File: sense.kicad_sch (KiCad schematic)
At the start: 36 parts, among them J6 Rudder, J7 End Stops, J8 Conn_01x02, J9 ISP, U4 XC6202P502FR-G, U6 LM317, U7 ATmega328P-AU, Y1 8mhz

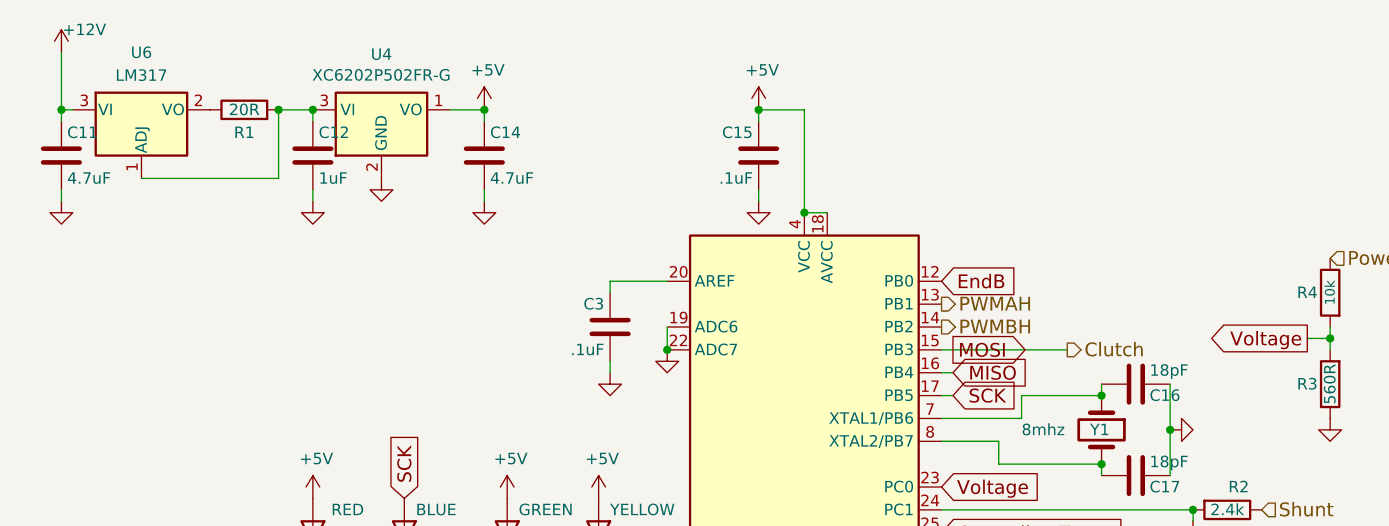
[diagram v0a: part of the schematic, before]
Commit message: Fixed almost all ERC errors and warnings (now 0 errors, 3 warnings)
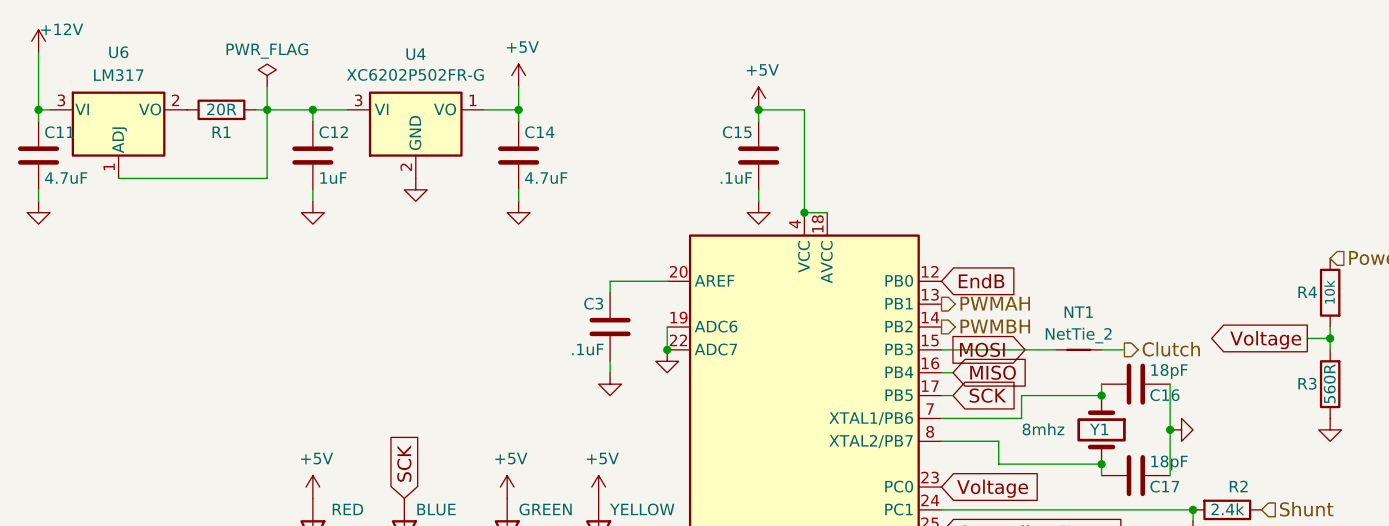
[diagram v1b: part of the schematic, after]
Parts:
- added NT1: NetTie_2, NetTie:NetTie-2_SMD_Pad0.5mm, symbol Device:NetTie_2
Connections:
- net MOSI: now also NT1.1
- new net Clutch: NT1.2
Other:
- moved on the sheet: C11, C14, R1, U4, U6

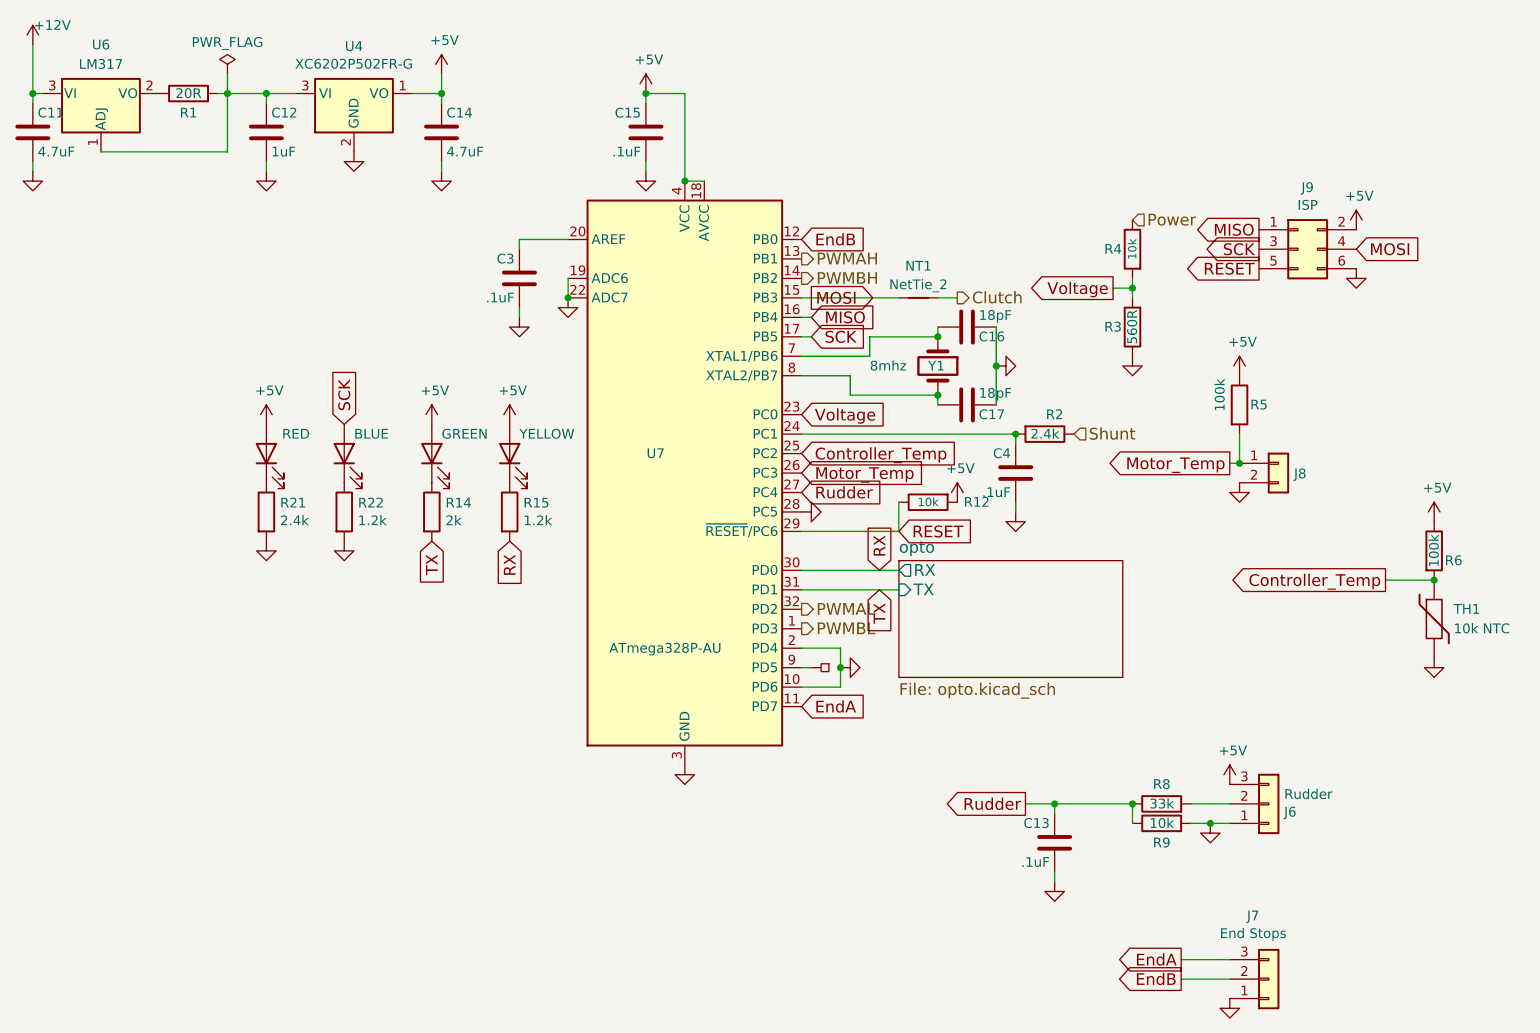
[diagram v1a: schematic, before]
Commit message: Cleaned LCSC part numbers out of datasheet field (and renamed 0.1u to 100n)
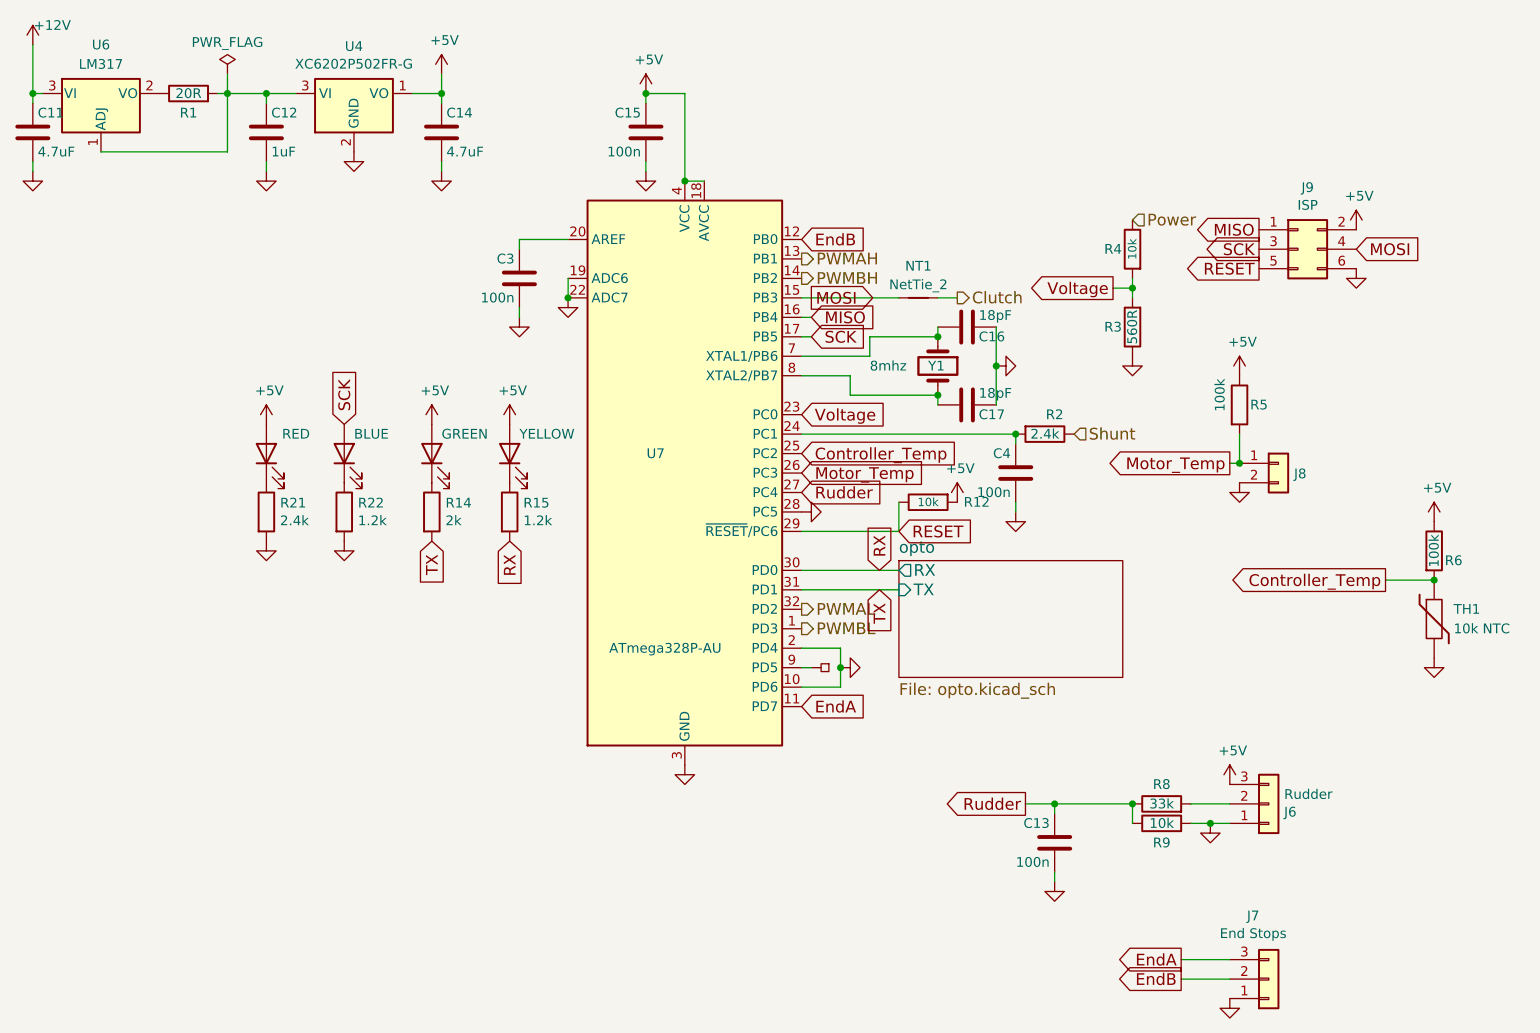
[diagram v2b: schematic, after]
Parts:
- C13, C15, C3, C4: value .1uF -> 100n
- TH1: LCSC C72672 -> *C72672, C51597
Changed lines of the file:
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@@
 			)
 		)
-		(property "Datasheet" "C51597, C72672"
+		(property "Datasheet" "~"
 			(at 218.44 100.33 0)
 			(effects
@@
 			)
 		)
-		(property "LCSC" "C72672"
+		(property "LCSC" "*C72672, C51597"
 			(at 218.44 100.33 0)
 			(effects
@@
 			)
 		)
-		(property "Value" ".1uF"
+		(property "Value" "100n"
 			(at 98.425 58.42 0)
 			(effects
@@
 			)
 		)
-		(property "Value" ".1uF"
+		(property "Value" "100n"
 			(at 114.935 39.37 0)
 			(effects
@@
 			)
 		)
-		(property "Value" ".1uF"
+		(property "Value" "100n"
 			(at 163.195 83.82 0)
 			(effects
@@
 			)
 		)
-		(property "Value" ".1uF"
+		(property "Value" "100n"
 			(at 168.275 132.08 0)
 			(effects

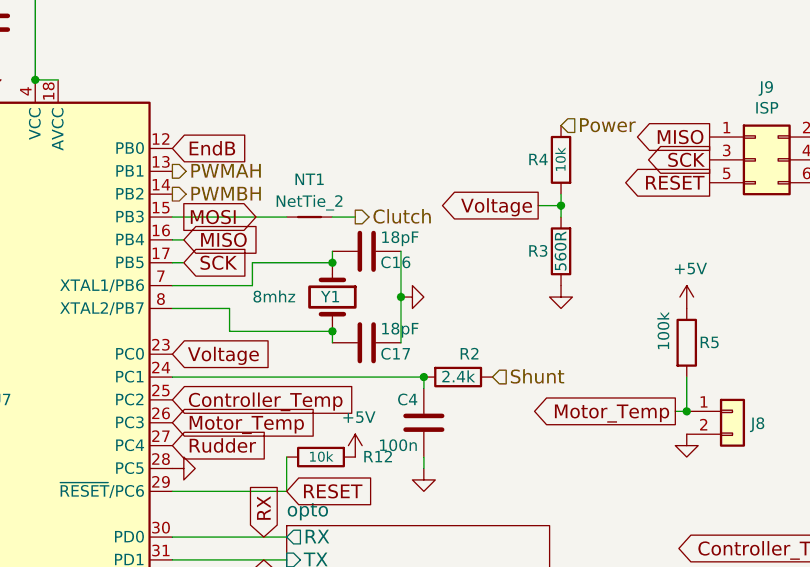
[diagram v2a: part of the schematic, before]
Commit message: Replace crystal caps with a JLC PCBA basic part (20pF instead of 18pF)
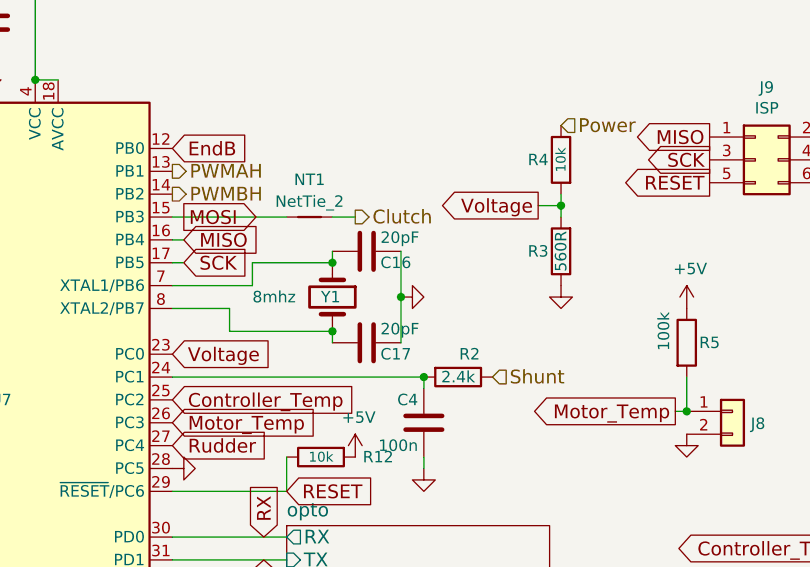
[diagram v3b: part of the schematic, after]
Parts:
- C16, C17: value 18pF -> 20pF; LCSC C1797 -> C1798
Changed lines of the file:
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@@
 			)
 		)
-		(property "Value" "18pF"
+		(property "Value" "20pF"
 			(at 159.004 70.866 90)
 			(effects
@@
 			)
 		)
-		(property "LCSC" "C1797"
+		(property "LCSC" "C1798"
 			(at 157.48 72.39 90)
 			(effects
@@
 			)
 		)
-		(property "Value" "18pF"
+		(property "Value" "20pF"
 			(at 159.004 60.706 90)
 			(effects
@@
 			)
 		)
-		(property "LCSC" "C1797"
+		(property "LCSC" "C1798"
 			(at 157.48 62.23 90)
 			(effects

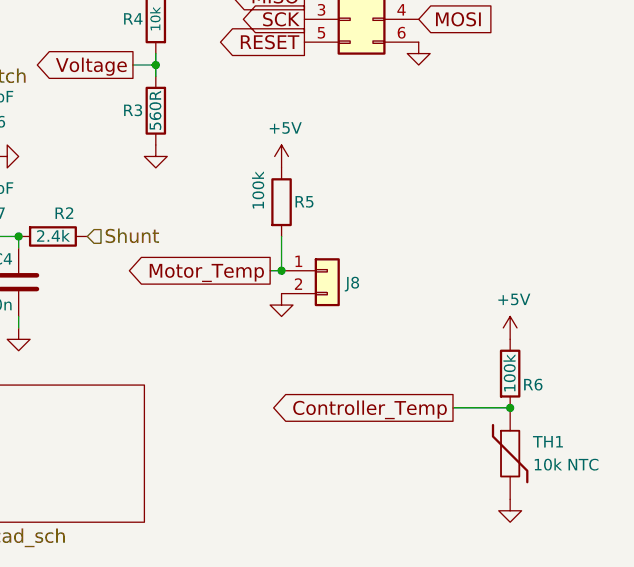
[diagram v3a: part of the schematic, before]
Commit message: Show motor temp on J8, the motor temp connector
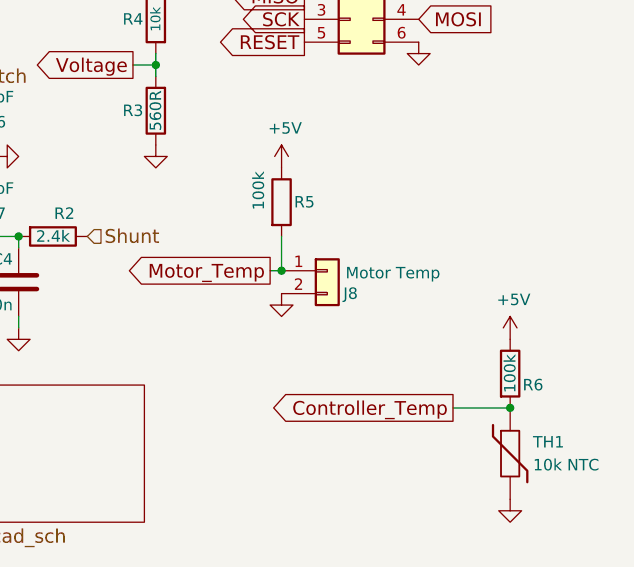
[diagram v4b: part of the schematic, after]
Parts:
- J8: value Conn_01x02 -> Motor Temp
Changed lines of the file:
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@@
 		(dnp no)
 		(property "Reference" "J8"
-			(at 200.152 81.3816 0)
+			(at 199.898 82.55 0)
 			(effects
 				(font
@@
 			)
 		)
-		(property "Value" "Conn_01x02"
-			(at 200.152 82.5246 0)
+		(property "Value" "Motor Temp"
+			(at 200.152 80.264 0)
 			(effects
 				(font
@@
 				)
 				(justify left)
-				(hide yes)
 			)
 		)

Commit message: Add MOSFET to switch a relay on the clutch output
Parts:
- J6, J7: LCSC (none) -> C19190477
- J8: LCSC (none) -> C7434479
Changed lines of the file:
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@@
+			)
+		)
+		(property "LCSC" "C7434479"
+			(at 198.12 80.01 0)
+			(effects
+				(font
+					(size 1.27 1.27)
+				)
+				(hide yes)
 			)
 		)
@@
 			)
 		)
+		(property "LCSC" "C19190477"
+			(at 196.85 124.46 0)
+			(effects
+				(font
+					(size 1.27 1.27)
+				)
+				(hide yes)
+			)
+		)
 		(pin "1"
 		)
@@
 			(at 196.85 147.32 0)
 			(effects
+				(font
+					(size 1.27 1.27)
+				)
+				(hide yes)
+			)
+		)
+		(property "LCSC" "C19190477"
+			(at 196.85 147.32 0)
+			(effects

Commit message: Tweaks to hand-load components for current availability
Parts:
- J8: LCSC C7434479 -> C7494857
- TH1: LCSC *C72672, C51597 -> C72672
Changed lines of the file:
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@@
 			)
 		)
-		(property "LCSC" "*C72672, C51597"
+		(property "LCSC" "C72672"
 			(at 218.44 100.33 0)
 			(effects
@@
 			)
 		)
-		(property "LCSC" "C7434479"
+		(property "LCSC" "C7494857"
 			(at 198.12 80.01 0)
 			(effects
